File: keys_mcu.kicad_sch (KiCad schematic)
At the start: 11 parts, among them J3 Conn_01x26_Socket, SW1 PWR, SW3 MUTE, SW4 PREV, SW5 PLAY_PAUSE, SW6 NEXT, U2 STM32G431CBUx, Y1 12MHz

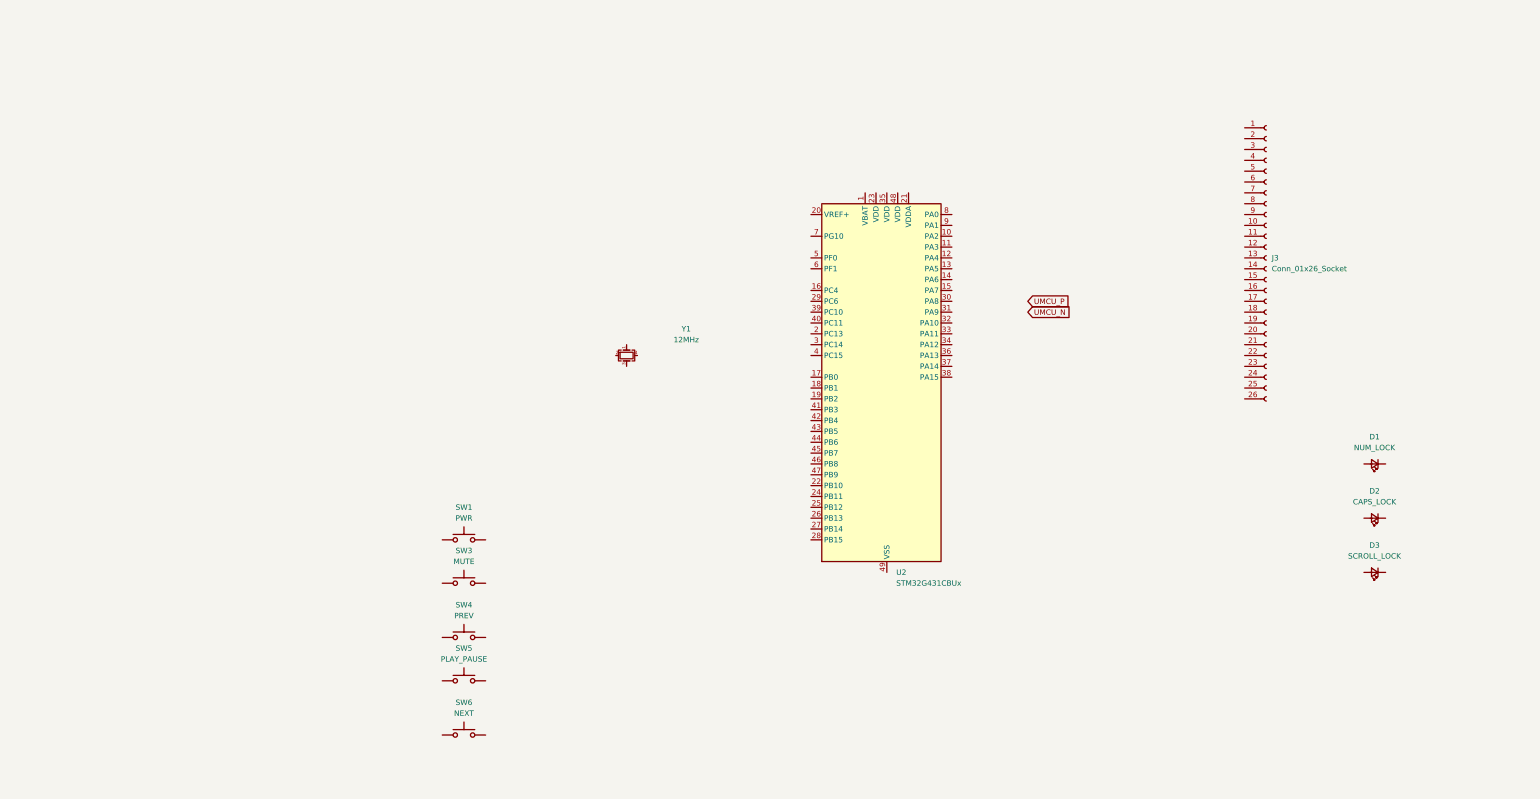
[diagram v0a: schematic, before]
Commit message: sch nearing completion.
usb side done.
needs mcu power supply sorting out.
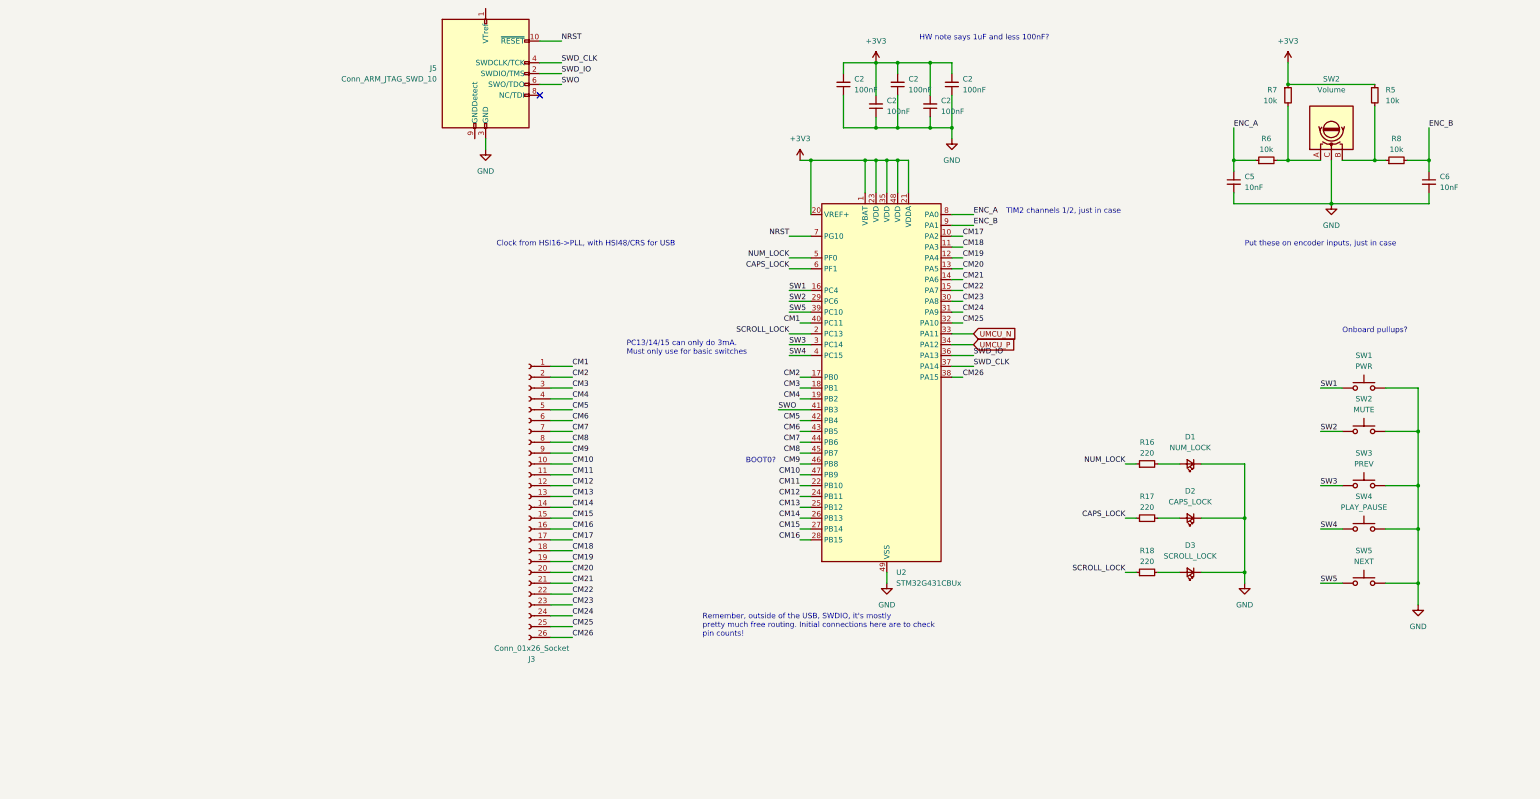
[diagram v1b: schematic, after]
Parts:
- removed Y1: 12MHz, Crystal:Crystal_SMD_3225-4Pin_3.2x2.5mm, symbol Device:Crystal_GND24_Small
- added C2 (x5): 100nF, Capacitor_SMD:C_0603_1608Metric, symbol Device:C_Small
- added C5, C6: 10nF, Capacitor_SMD:C_0603_1608Metric, symbol Device:C_Small
- added J5: Conn_ARM_JTAG_SWD_10, Connector_PinHeader_1.27mm:PinHeader_2x05_P1.27mm_Vertical_SMD, symbol Connector:Conn_ARM_JTAG_SWD_10
- added R16, R17, R18: 220, Resistor_SMD:R_0603_1608Metric, symbol Device:R_Small
- added R5, R6, R7, R8: 10k, Resistor_SMD:R_0603_1608Metric, symbol Device:R_Small
- added SW2: Volume, symbol Device:RotaryEncoder
- U2: jlc-basic (none) -> 0
- renumbered SW3 to SW2, SW4 to SW3, SW5 to SW4, SW6 to SW5
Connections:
- net UMCU_N: now also U2.33 (PA11)
- net UMCU_P: now also U2.34 (PA12)
- net SW1: now reaches SW1.1
- net SW1: now also U2.16 (PC4)
- net GND: now reaches SW1.2
- net GND: now also D1.1 (K), D2.1 (K), D3.1 (K), SW2.2, SW3.2, SW4.2, SW5.2, U2.49 (VSS), C2.1, C2.1, C2.1, C2.1, C2.1, C5.2, C6.2, J5.3 (GND), J5.5 (GND), SW2.C
- net SW2: now reaches SW2.1
- net SW2: now also U2.29 (PC6)
- net SW5: now reaches SW5.1
- net SW5: now also U2.39 (PC10)
- net at D3.2 (A): now also R18.2
- net SW4: now reaches SW4.1
- net SW4: now also U2.4 (PC15)
- net CM1: now reaches J3.1 (Pin_1)
- net CM1: now also U2.40 (PC11)
- net CM10: now reaches J3.10 (Pin_10)
- net CM10: now also U2.47 (PB9)
- net CM11: now reaches J3.11 (Pin_11)
- net CM11: now also U2.22 (PB10)
- net CM12: now reaches J3.12 (Pin_12)
- net CM12: now also U2.24 (PB11)
- net CM13: now reaches J3.13 (Pin_13)
- net CM13: now also U2.25 (PB12)
- net CM14: now reaches J3.14 (Pin_14)
- net CM14: now also U2.26 (PB13)
- net CM15: now reaches J3.15 (Pin_15)
- net CM15: now also U2.27 (PB14)
- net CM16: now reaches J3.16 (Pin_16)
- net CM16: now also U2.28 (PB15)
- net CM17: now reaches J3.17 (Pin_17)
- net CM17: now also U2.10 (PA2)
- net CM18: now reaches J3.18 (Pin_18)
- net CM18: now also U2.11 (PA3)
- net CM19: now reaches J3.19 (Pin_19)
- net CM19: now also U2.12 (PA4)
- net CM2: now reaches J3.2 (Pin_2)
- net CM2: now also U2.17 (PB0)
- net CM20: now reaches J3.20 (Pin_20)
- net CM20: now also U2.13 (PA5)
- net CM21: now reaches J3.21 (Pin_21)
- net CM21: now also U2.14 (PA6)
- net CM22: now reaches J3.22 (Pin_22)
- net CM22: now also U2.15 (PA7)
- net CM23: now reaches J3.23 (Pin_23)
- net CM23: now also U2.30 (PA8)
- net CM24: now reaches J3.24 (Pin_24)
- net CM24: now also U2.31 (PA9)
- net CM25: now reaches J3.25 (Pin_25)
- net CM25: now also U2.32 (PA10)
- net CM26: now reaches J3.26 (Pin_26)
- net CM26: now also U2.38 (PA15)
- net CM3: now reaches J3.3 (Pin_3)
- net CM3: now also U2.18 (PB1)
- net CM4: now reaches J3.4 (Pin_4)
- net CM4: now also U2.19 (PB2)
- net CM5: now reaches J3.5 (Pin_5)
- net CM5: now also U2.42 (PB4)
- net CM6: now reaches J3.6 (Pin_6)
- net CM6: now also U2.43 (PB5)
- net CM7: now reaches J3.7 (Pin_7)
- net CM7: now also U2.44 (PB6)
- net CM8: now reaches J3.8 (Pin_8)
- net CM8: now also U2.45 (PB7)
- net CM9: now reaches J3.9 (Pin_9)
- net CM9: now also U2.46 (PB8)
- net at D1.2 (A): now also R16.2
- net SW3: now reaches SW3.1
- net SW3: now also U2.3 (PC14)
- net +3V3: now reaches U2.1 (VBAT)
- net +3V3: now also U2.20 (VREF+), U2.21 (VDDA), U2.23 (VDD), U2.35 (VDD), U2.48 (VDD), C2.2, C2.2, C2.2, C2.2, C2.2, R5.1, R7.1
- net SCROLL_LOCK: now reaches U2.2 (PC13)
- net SCROLL_LOCK: now also R18.1
- net SWD_IO: now reaches U2.36 (PA13)
- net SWD_IO: now also J5.2 (SWDIO/TMS)
- net SWD_CLK: now reaches U2.37 (PA14)
- net SWD_CLK: now also J5.4 (SWDCLK/TCK)
- net SWO: now reaches U2.41 (PB3)
- net SWO: now also J5.6 (SWO/TDO)
- net NUM_LOCK: now reaches U2.5 (PF0)
- net NUM_LOCK: now also R16.1
- net CAPS_LOCK: now reaches U2.6 (PF1)
- net CAPS_LOCK: now also R17.1
- net NRST: now reaches U2.7 (PG10)
- net NRST: now also J5.10 (~{RESET})
- net ENC_A: now reaches U2.8 (PA0)
- net ENC_A: now also C5.1, R6.1
- net ENC_B: now reaches U2.9 (PA1)
- net ENC_B: now also C6.1, R8.2
- net at D2.2 (A): now also R17.2
- new net: R6.2, R7.2, SW2.A
- new net: R5.2, R8.1, SW2.B
- no-connect marks 0 -> 1
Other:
- note added: "BOOT0?"
- note added: "Clock from HSI16->PLL, with HSI48/CRS for USB"
- note added: "HW note says 1uF and less 100nF?"
- note added: "Onboard pullups?"
- note added: "PC13/14/15 can only do 3mA. Must only use for basic switches"
- note added: "Put these on encoder inputs, just in case"
- note added: "Remember, outside of the USB, SWDIO, it's mostly pretty much free routing. Initial connections here are to check pin counts!"
- note added: "TIM2 channels 1/2, just in case"
- moved on the sheet: D1, D2, D3, J3, SW1, SW2, SW3, SW4, SW5

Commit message: schematic "done" footprints all assigned
Need working calipers to start getting the board outline and fixed
positions, but ... mostly there?

schematic needs "polish" now, more introductions, cleaner text layouts,
probably more optional test points, throw more caps at it.
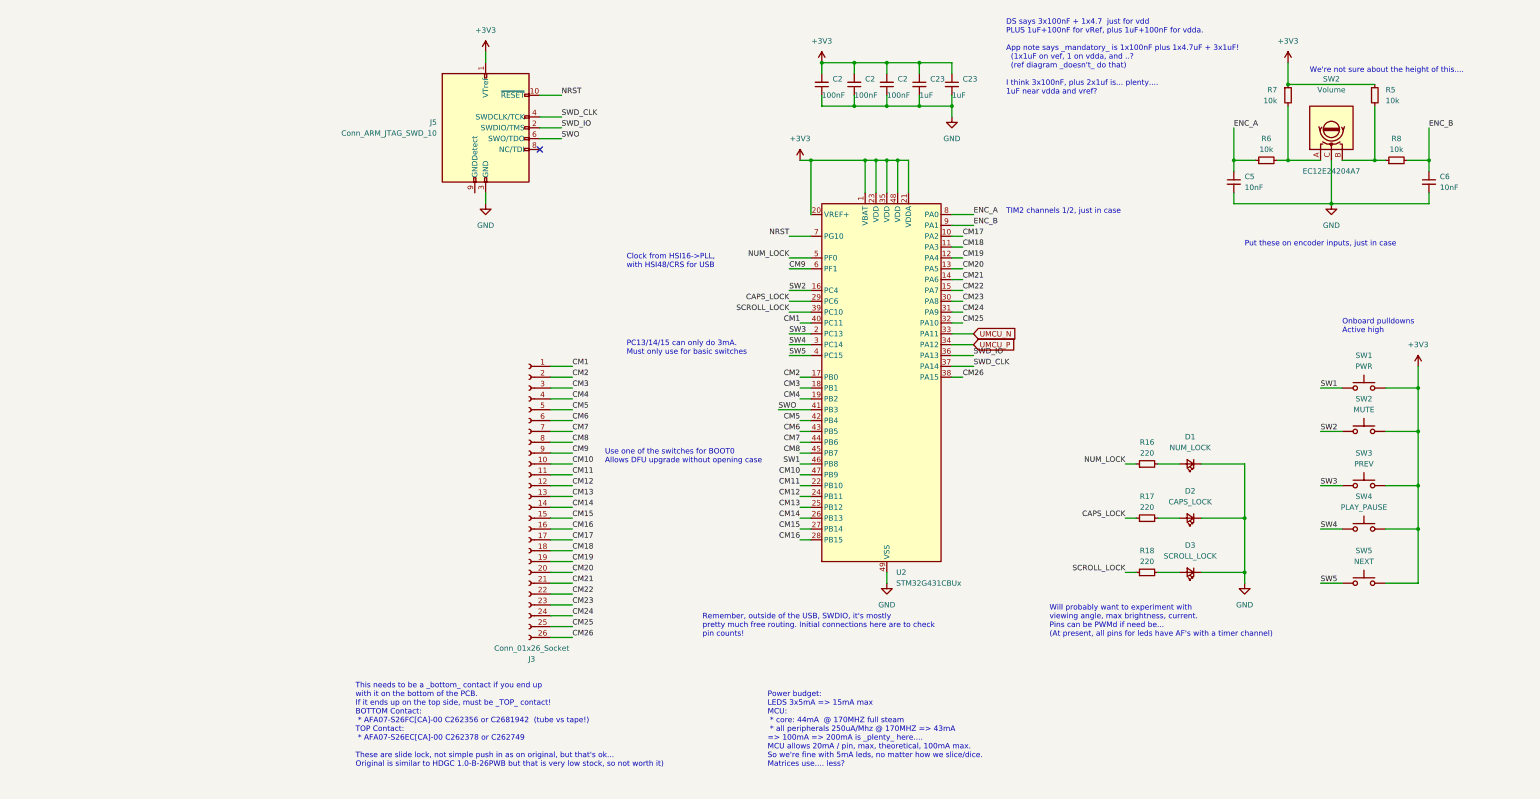
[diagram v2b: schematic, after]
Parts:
- removed C2 (x3): 100nF, Capacitor_SMD:C_0603_1608Metric, symbol Device:C_Small
- added C2: 100nF, Capacitor_SMD:C_0603_1608Metric, symbol Device:C_Small
- added C23 (x2): 1uF, Capacitor_SMD:C_0603_1608Metric, symbol Device:C_Small
- D1, D2, D3: footprint (none) -> LED_THT:LED_D5.0mm; MPN (none) -> 333-2SURC/S530-A3; jlc-basic (none) -> 0; lcsc# (none) -> C125756
- J3: footprint (none) -> Connector_FFC-FPC:TE_2-84952-6_1x26-1MP_P1.0mm_Horizontal; MPN (none) -> AFA07-S26FCC-00; jlc-basic (none) -> 0
- SW1, SW2, SW3, SW4, SW5: footprint (none) -> Button_Switch_SMD:SW_SPST_TL3342; MPN (none) -> TS-1187A-B-A-B; jlc-basic (none) -> 1; lcsc# C967783 -> C318884
- SW2: footprint (none) -> Rotary_Encoder:RotaryEncoder_Alps_EC12E_Vertical_H20mm_CircularMountingHoles; MPN (none) -> EC12E24204A7; lcsc# (none) -> C470597
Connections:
- net +3V3: now also J5.1 (VTref), SW1.2, SW2.2, SW3.2, SW4.2, SW5.2, C2.2, C23.1, C23.1
- net CAPS_LOCK: now also U2.29 (PC6); no longer U2.6 (PF1)
- net CM9: now also U2.6 (PF1); no longer U2.46 (PB8)
- net GND: now also C2.1, C23.2, C23.2; no longer SW1.2, SW2.2, SW3.2, SW4.2, SW5.2
- net SCROLL_LOCK: now also U2.39 (PC10); no longer U2.2 (PC13)
- net SW1: now also U2.46 (PB8); no longer U2.16 (PC4)
- net SW2: now also U2.16 (PC4); no longer U2.29 (PC6)
- net SW3: now also U2.2 (PC13); no longer U2.3 (PC14)
- net SW4: now also U2.3 (PC14); no longer U2.4 (PC15)
- net SW5: now also U2.4 (PC15); no longer U2.39 (PC10)
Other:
- note added: "DS says 3x100nF + 1x4.7 just for vdd PLUS 1uF+100nF for vRef, plus 1uF+100nF for vdda. App note says _mandatory_ is 1x100nF plus 1x4.7uF + 3x1uF! (1x1uF on vef, 1 on vdda, and ..? (ref diagram _doesn't_ do that) I think 3x100nF, plus 2x1uf is... plenty.... 1uF near vdda and vref?"
- note added: "Onboard pulldowns Active high"
- note added: "Power budget: LEDS 3x5mA => 15mA max MCU: * core: 44mA @ 170MHZ full steam * all peripherals 250uA/Mhz @ 170MHZ => 43mA => 100mA => 200mA is _plenty_ here.... MCU allows 20mA / pin, max, theoretical, 100mA max. So we're fine with 5mA leds, no matter how we slice/dice. Matrices use.... less?"
- note added: "This needs to be a _bottom_ contact if you end up with it on the bottom of the PCB. If it ends up on the top side, must be _TOP_ contact! BOTTOM Contact: * AFA07-S26FC[CA]-00 C262356 or C2681942 (tube vs tape!) TOP Contact: * AFA07-S26EC[CA]-00 C262378 or C262749 These are slide lock, not simple push in as on original, but that's ok... Original is similar to HDGC 1.0-B-26PWB but that is very low 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"
- note added: "Use one of the switches for BOOT0 Allows DFU upgrade without opening case"
- note added: "We're not sure about the height of this...."
- note added: "Will probably want to experiment with viewing angle, max brightness, current. Pins can be PWMd if need be... (At present, all pins for leds have AF's with a timer channel)"
- note removed: "BOOT0?"
- note removed: "HW note says 1uF and less 100nF?"
- note removed: "Onboard pullups?"
- moved on the sheet: C2, J5

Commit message: add "bonus" can transceiver ;)
this is so we can use the round 1 protos for another project...

also: replace srv05 with an alternate, also jlc preferred, but cheaper
part.  Update power budgets.

We've done some initial work with the pcb, but we're running into weird
kicad wx bugs, so we're going to save it all here, and commit, and
perhaps continue with 7.99.....
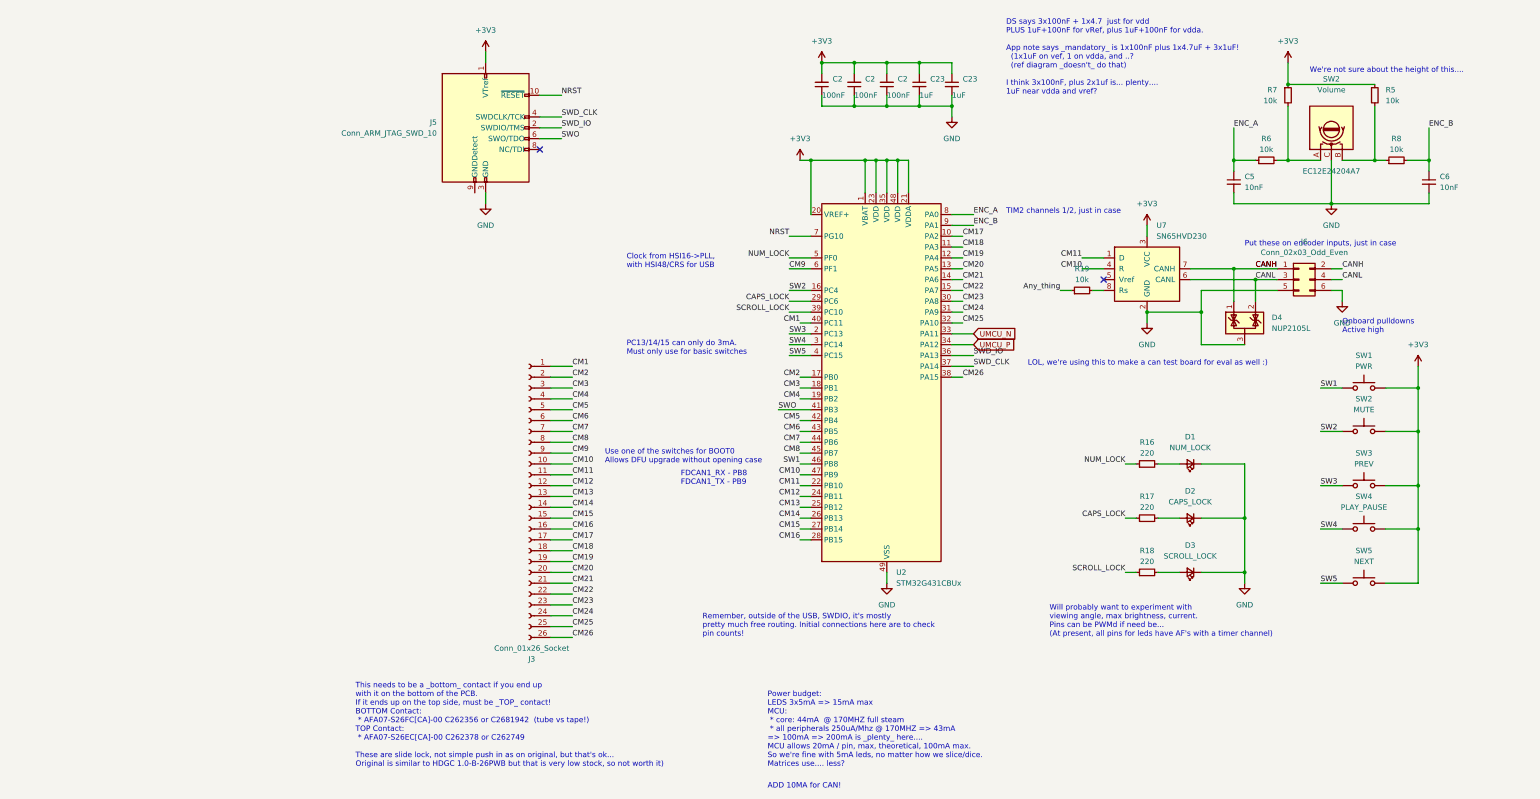
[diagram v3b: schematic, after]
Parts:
- added D4: NUP2105L, Package_TO_SOT_SMD:SOT-23, symbol Power_Protection:NUP2105L
- added J6: Conn_02x03_Odd_Even, Connector_PinHeader_2.54mm:PinHeader_2x03_P2.54mm_Vertical, symbol Connector_Generic:Conn_02x03_Odd_Even
- added R19: 10k, Resistor_SMD:R_0603_1608Metric, symbol Device:R_Small
- added U7: SN65HVD230, Package_SO:SOIC-8_3.9x4.9mm_P1.27mm, symbol Interface_CAN_LIN:SN65HVD230
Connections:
- net +3V3: now also U7.3 (VCC)
- net CM10: now also U7.4 (R)
- net CM11: now also U7.1 (D)
- net GND: now also D4.3 (A), J6.5 (Pin_5), J6.6 (Pin_6), U7.2 (GND)
- new net: R19.2, U7.8 (Rs)
- new net Any_thing: R19.1
- new net CANH: D4.1 (K), J6.1 (Pin_1), J6.2 (Pin_2), U7.7 (CANH)
- new net CANL: D4.2 (K), J6.3 (Pin_3), J6.4 (Pin_4), U7.6 (CANL)
- no-connect marks 1 -> 2
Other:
- note added: "ADD 10MA for CAN!"
- note added: "FDCAN1_RX - PB8 FDCAN1_TX - PB9"
- note added: "LOL, we're using this to make a can test board for eval as well :)"
